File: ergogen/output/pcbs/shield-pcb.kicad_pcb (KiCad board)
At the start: 2 copper layers, 118.1 x 90.8 mm, 26 parts

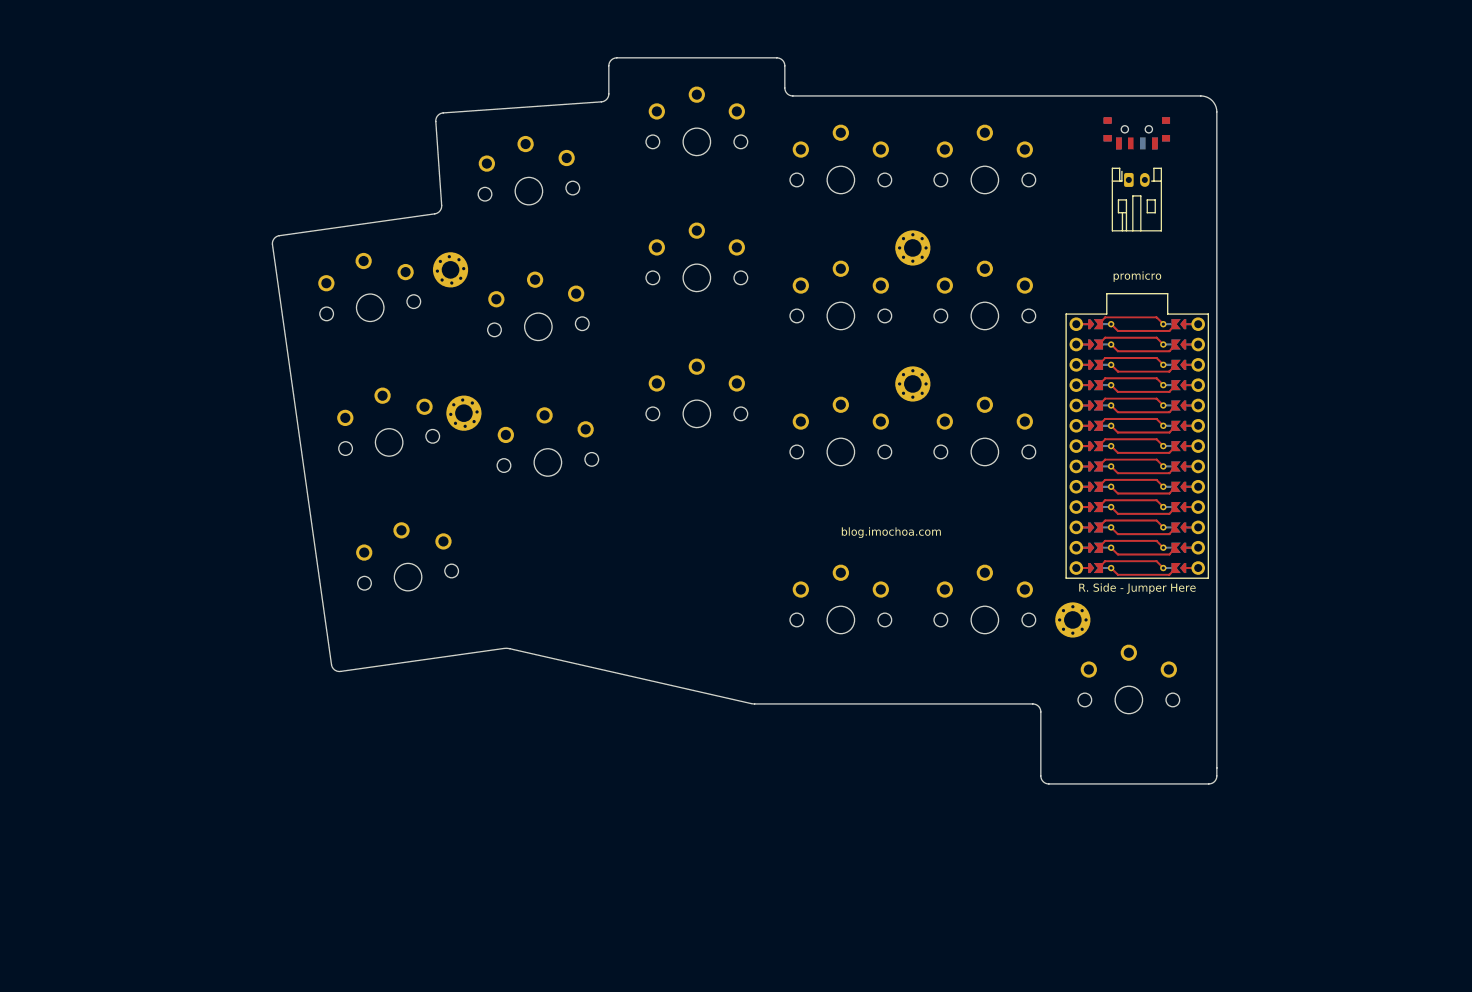
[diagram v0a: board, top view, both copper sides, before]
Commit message: added current cases outlines and pcbs
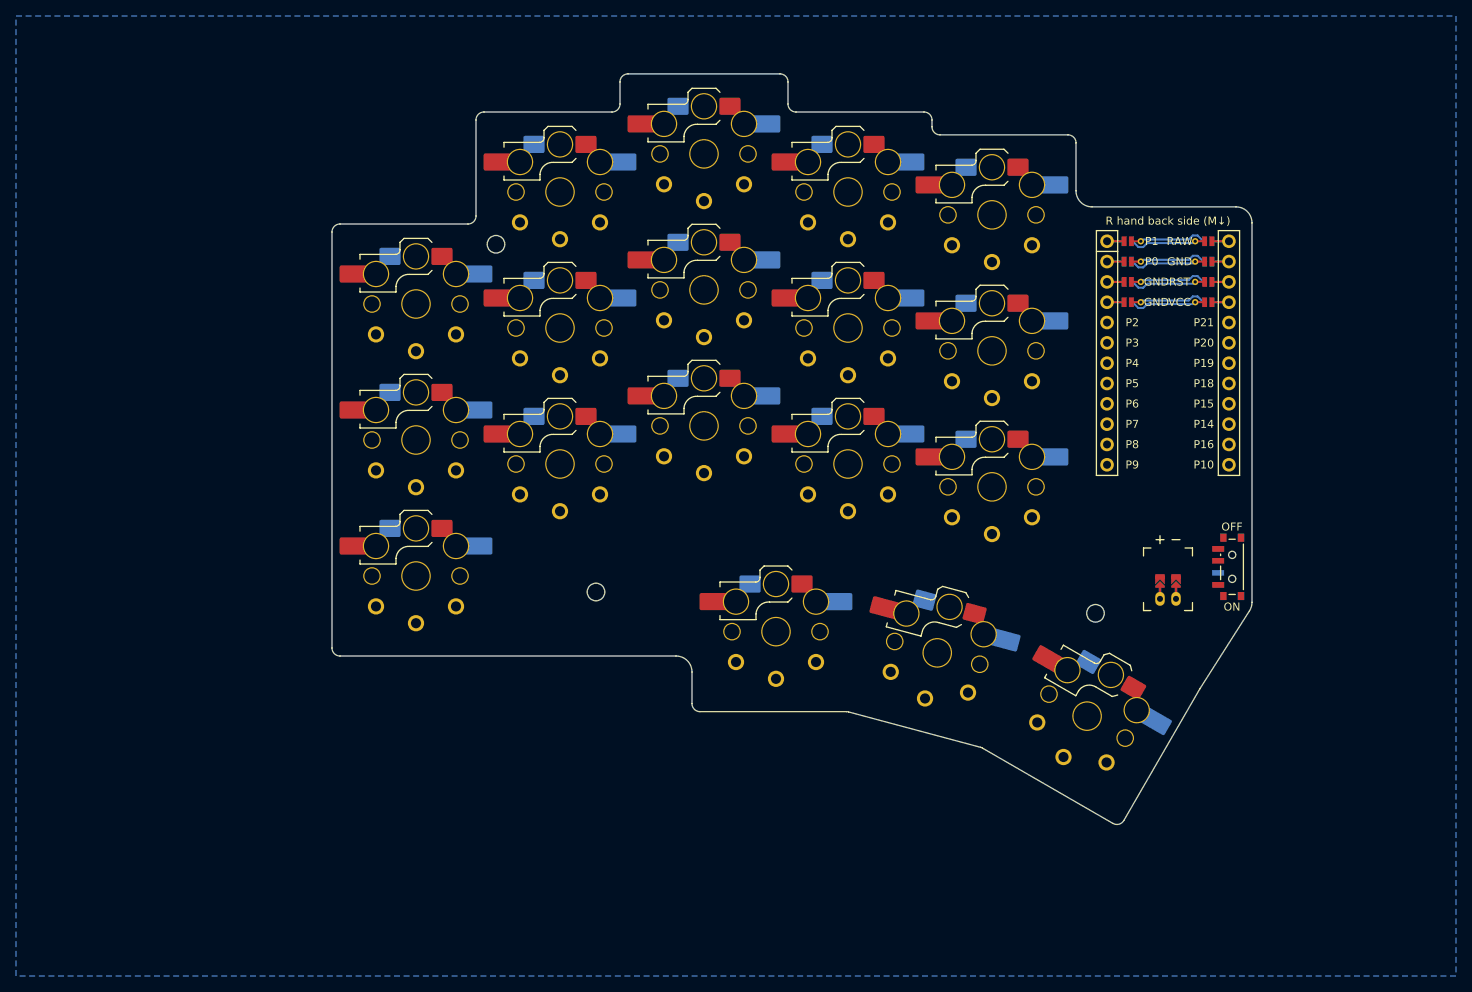
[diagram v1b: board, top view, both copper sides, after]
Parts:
- removed MCU: , ProMicro
- removed T1: , Button_Switch_SMD:SW_SPDT_PCM12
- removed _10, _6, _7, _8, _9: , MountingHole_2.2mm_M2_Pad_Via
- removed _2: , Connector_JST:JST_PH_S2B-PH-K_1x02_P2.00mm_Horizontal
- added JST1: , ceoloide:battery_connector_jst_ph_2, F.Cu at (244.0, 152.9)
- added MCU1: , ceoloide:mcu_supermini_nrf52840, F.Cu at (244.0, 120.9)
- added MH1: , ceoloide:mounting_hole_npth, F.Cu at (160.0, 108.5)
- added MH2: , ceoloide:mounting_hole_npth, F.Cu at (172.5, 152.0)
- added MH3: , ceoloide:mounting_hole_npth, F.Cu at (234.9, 154.7)
- added PWR1: , ceoloide:power_switch_smd_side, F.Cu at (252.0, 148.9)
- S1, S10, S11, S12, S13, S14, S15, S16, S17, S18, S2, S3, S4, S5, S6, S7, S8, S9: footprint PG1350 -> ceoloide:switch_choc_v1_v2; moved to B.Cu
- moved S16 8.24 mm to (195.0, 157.0)
- moved S17 7.23 mm to (215.2, 159.6), turned to -15 degrees
- moved S3 5.74 mm to (150.0, 116.0), turned to 0 degrees
- moved S18 5.60 mm to (233.9, 167.5), turned to -30 degrees
- moved S13 4.45 mm to (222.0, 138.9)
- moved S14 4.45 mm to (222.0, 121.9)
- moved S15 4.45 mm to (222.0, 104.9)
- moved S6 3.89 mm to (168.0, 102.0), turned to 0 degrees
- moved S2 3.37 mm to (150.0, 133.0), turned to 0 degrees
- moved S5 2.71 mm to (168.0, 119.0), turned to 0 degrees
- moved S7 1.75 mm to (186.0, 131.2)
- moved S8 1.75 mm to (186.0, 114.2)
- moved S9 1.75 mm to (186.0, 97.2)
- moved S10 1.75 mm to (204.0, 136.0)
- moved S11 1.75 mm to (204.0, 119.0)
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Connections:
- S1 pad 1: GND -> grid-zn_pinky_bottom
- S1 pad 2: grid-zn_pinky_bottom -> GND
- S10 pad 1: GND -> grid-zn_index_bottom
- S10 pad 2: grid-zn_index_bottom -> GND
- S11 pad 1: GND -> grid-zn_index_home
- S11 pad 2: grid-zn_index_home -> GND
- S12 pad 1: GND -> grid-zn_index_top
- S12 pad 2: grid-zn_index_top -> GND
- S13 pad 1: GND -> grid-zn_inner_bottom
- S13 pad 2: grid-zn_inner_bottom -> GND
- S14 pad 1: GND -> grid-zn_inner_home
- S14 pad 2: grid-zn_inner_home -> GND
- S15 pad 1: GND -> grid-zn_inner_top
- S15 pad 2: grid-zn_inner_top -> GND
- S16 pad 1: GND -> thumb-zn_near_thumb
- S16 pad 2: thumb-zn_near_thumb -> GND
- S17 pad 1: GND -> thumb-zn_home_thumb
- S17 pad 2: thumb-zn_home_thumb -> GND
- S18 pad 1: GND -> thumb-zn_far_thumb
- S18 pad 2: thumb-zn_far_thumb -> GND
- S2 pad 1: GND -> grid-zn_pinky_home
- S2 pad 2: grid-zn_pinky_home -> GND
- S3 pad 1: GND -> grid-zn_pinky_top
- S3 pad 2: grid-zn_pinky_top -> GND
- S4 pad 1: GND -> grid-zn_ring_bottom
- S4 pad 2: grid-zn_ring_bottom -> GND
- S5 pad 1: GND -> grid-zn_ring_home
- S5 pad 2: grid-zn_ring_home -> GND
- S6 pad 1: GND -> grid-zn_ring_top
- S6 pad 2: grid-zn_ring_top -> GND
- S7 pad 1: GND -> grid-zn_middle_bottom
- S7 pad 2: grid-zn_middle_bottom -> GND
- S8 pad 1: GND -> grid-zn_middle_home
- S8 pad 2: grid-zn_middle_home -> GND
- S9 pad 1: GND -> grid-zn_middle_top
- S9 pad 2: grid-zn_middle_top -> GND
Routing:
- net (no net): track 371.4 -> 111.0 mm
- net JST1_2: track 0.00 -> 3.60 mm
- net JST1_1: track 0.00 -> 3.60 mm
- added copper zone on B.Cu, net GND
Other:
- board size 118.1 x 90.8 mm -> 115 x 93.8 mm
- net class Default removed
- board text removed: "blog.imochoa.com"
